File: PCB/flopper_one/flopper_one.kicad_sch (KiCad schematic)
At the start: 13 parts, among them J1 To PN532 ->, J2 <- ST7789, Q1 2N2219, SW1 SW_Omron_B3FS, SW2 SW_Omron_B3FS, SW3 SW_Omron_B3FS, SW4 SW_Omron_B3FS, SW5 SW_Omron_B3FS

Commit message: adfsdfd
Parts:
- U2: footprint ESP32_30pin -> wroom:MODULE_DEVKIT_V1_ESP32-WROOM-32
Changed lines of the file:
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@@
 			)
 		)
-		(property "Footprint" "ESP32_30pin"
+		(property "Footprint" "wroom:MODULE_DEVKIT_V1_ESP32-WROOM-32"
 			(at 156.21 89.5349 0)
 			(effects

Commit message: use labels
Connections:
- net VCC: no longer R1.2, U2.16 (3.3v)
- net P4: now reaches SW4.1, U2.4 (GPIO12)
- net P1: now reaches SW1.1, U2.5 (GPIO14)
- net P2: now reaches SW2.1, U2.6 (GPIO27)
- net P3: now reaches SW3.1, U2.7 (GPIO26)
- net P5: now reaches SW5.1, U2.8 (GPIO25)
- net SCL renamed SCL1
- net SCL1: no longer J2.3 (Pin_3), U2.24 (GPIO18)
- net SDA renamed SDA1
- net SDA1: no longer J2.4 (Pin_4), U2.25 (GPIO19)
- new net SCL2: J2.3 (Pin_3), U2.24 (GPIO18)
- new net SDA2: J2.4 (Pin_4), U2.25 (GPIO19)
- new net vcc: R1.2, U2.16 (3.3v)

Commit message: routed the pcb
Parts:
- J1: footprint Connector_PinHeader_1.00mm:PinHeader_1x04_P1.00mm_Vertical -> Connector_PinHeader_2.54mm:PinHeader_1x04_P2.54mm_Vertical
- J2: footprint Connector_PinHeader_1.00mm:PinHeader_1x07_P1.00mm_Vertical -> Connector_PinHeader_2.54mm:PinHeader_1x07_P2.54mm_Vertical
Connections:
- net vcc is gone; now on net VCC: R1.2, U2.16 (3.3v)
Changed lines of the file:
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@@
 		)
 	)
-	(label "vcc"
+	(label "VCC"
 		(at 147.32 72.39 0)
 		(effects
@@
 			)
 		)
-		(property "Footprint" "Connector_PinHeader_1.00mm:PinHeader_1x07_P1.00mm_Vertical"
+		(property "Footprint" "Connector_PinHeader_2.54mm:PinHeader_1x07_P2.54mm_Vertical"
 			(at 63.5 102.87 0)
 			(effects
@@
 			)
 		)
-		(property "Footprint" "Connector_PinHeader_1.00mm:PinHeader_1x04_P1.00mm_Vertical"
+		(property "Footprint" "Connector_PinHeader_2.54mm:PinHeader_1x04_P2.54mm_Vertical"
 			(at 63.5 77.47 0)
 			(effects

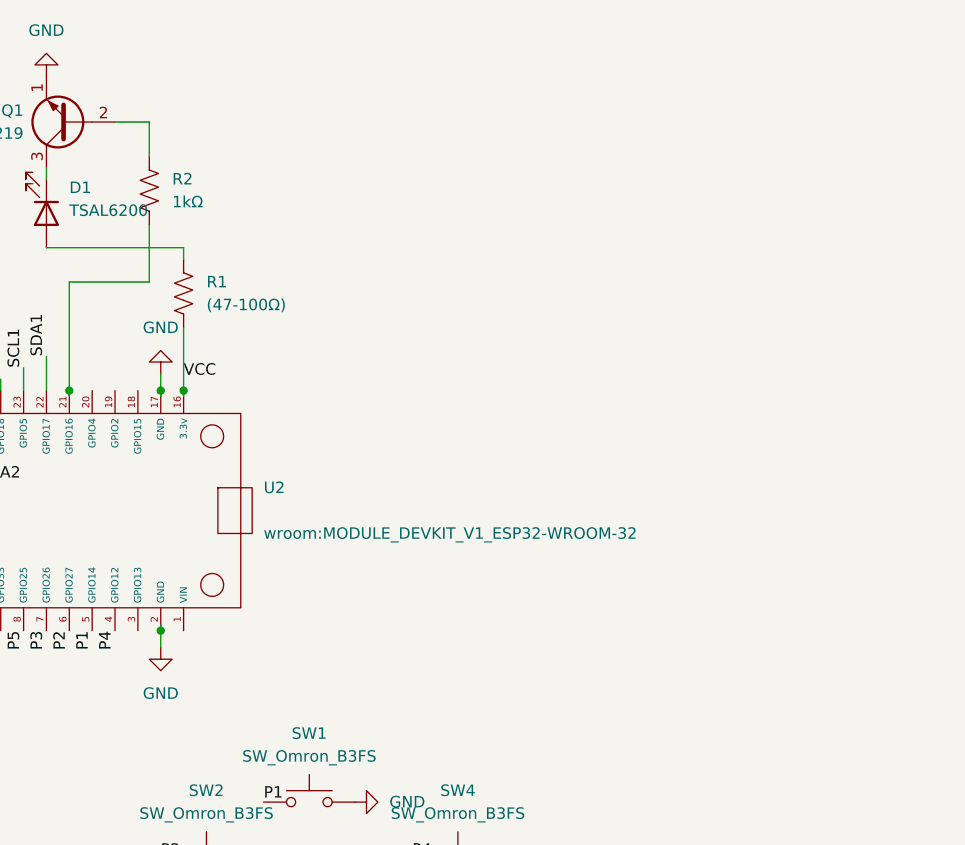
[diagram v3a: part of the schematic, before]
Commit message: add battery
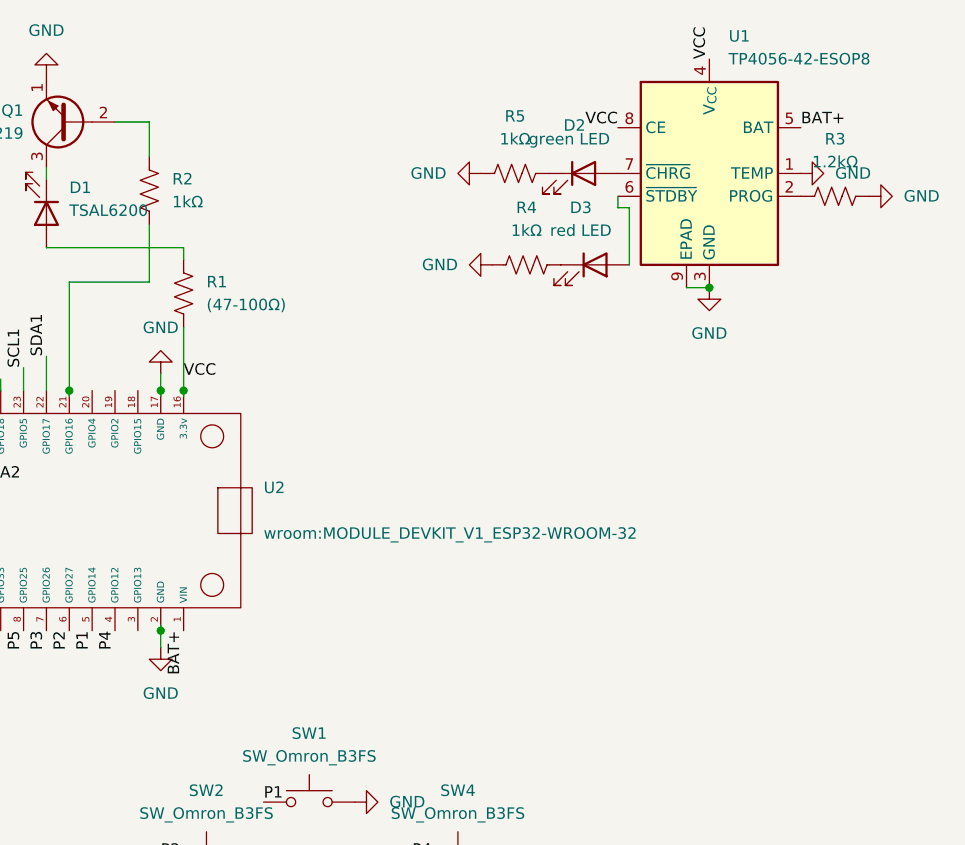
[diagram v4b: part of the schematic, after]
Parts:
- added D2: green LED, LED_THT:LED_D5.0mm, symbol Device:LED
- added D3: red LED, LED_THT:LED_D5.0mm, symbol Device:LED
- added R3: 1.2kΩ, Resistor_THT:R_Axial_DIN0207_L6.3mm_D2.5mm_P7.62mm_Horizontal, symbol Device:R_US
- added R4, R5: 1kΩ, Resistor_THT:R_Axial_DIN0207_L6.3mm_D2.5mm_P7.62mm_Horizontal, symbol Device:R_US
- added U1: TP4056-42-ESOP8, Package_SO:SOIC-8-1EP_3.9x4.9mm_P1.27mm_EP2.41x3.3mm_ThermalVias, symbol Battery_Management:TP4056-42-ESOP8
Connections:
- net GND: now also R3.2, R4.1, R5.1, U1.1 (TEMP), U1.3 (GND), U1.9 (EPAD)
- net VCC: now also U1.4 (V_{CC}), U1.8 (CE)
- net BAT+: now reaches U2.1 (VIN)
- net BAT+: now also U1.5 (BAT)
- new net: D3.1 (K), R4.2
- new net: D3.2 (A), U1.6 (~{STDBY})
- new net: R3.1, U1.2 (PROG)
- new net: D2.1 (K), R5.2
- new net: D2.2 (A), U1.7 (~{CHRG})

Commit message: added like power circuits fr
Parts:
- added C1: 10uf, Capacitor_THT:CP_Axial_L10.0mm_D4.5mm_P15.00mm_Horizontal, symbol Device:C_Small
- added U3: MT3608 module, MT3608:hw-045, symbol hw-045:hw-045
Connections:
- net BAT+: now also C1.1, U3.1 (VIN+); no longer U2.1 (VIN)
- net GND: now also D2.2 (A), D3.2 (A), C1.2, U3.2 (VIN-), U3.4 (VOUT-); no longer R4.1, R5.1
- net at U1.6 (~{STDBY}): now also R4.1; no longer D3.2 (A)
- net at U1.7 (~{CHRG}): now also R5.1; no longer D2.2 (A)
- new net VIN: U2.1 (VIN), U3.3 (VOUT+)
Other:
- moved on the sheet: D2, D3, R4, R5

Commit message: fix battery rq
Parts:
- removed U3: MT3608 module, MT3608:hw-045, symbol hw-045:hw-045
- added U4: hw-045, MT3608:hw-045, symbol hw-045:hw-045
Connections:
- net BAT+: now also U4.4 (VIN+)
- net GND: now also U4.2 (VOUT-), U4.3 (VIN-)
- net VIN: now also U4.1 (VOUT+)
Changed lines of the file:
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@@
+		)
+	)
+	(label "VIN"
+		(at 205.74 140.97 180)
+		(effects
+			(font
+				(size 1.27 1.27)
+			)
+			(justify right bottom)
 		)
 	)
@@
 		)
 	)
-	(label "BAT+"
-		(at 204.47 121.92 180)
-		(effects
-			(font
-				(size 1.27 1.27)
-			)
-			(justify right bottom)
-		)
-	)
 	(label "P1"
 		(at 156.21 119.38 0)
@@
 		)
 	)
-	(label "VIN"
-		(at 232.41 124.46 0)
-		(effects
-			(font
-				(size 1.27 1.27)
-			)
-			(justify left bottom)
-		)
-	)
 	(label "P5"
 		(at 106.68 125.73 0)
@@
 		)
 	)
+	(label "BAT+"
+		(at 233.68 140.97 0)
+		(effects
+			(font
+				(size 1.27 1.27)
+			)
+			(justify left bottom)
+		)
+	)
 	(label "SDA2"
 		(at 124.46 83.82 0)
@@
 	(symbol
 		(lib_id "power:GND")
-		(at 232.41 121.92 180)
-		(unit 1)
-		(exclude_from_sim no)
-		(in_bom yes)
-		(on_board yes)
-		(dnp no)
-		(fields_autoplaced yes)
-		(property "Reference" "#PWR019"
-			(at 232.41 115.57 0)
-			(effects
-				(font
-					(size 1.27 1.27)
-				)
-				(hide yes)
-			)
-		)
-		(property "Value" "GND"
-			(at 232.41 116.84 0)
-			(effects
-				(font
-					(size 1.27 1.27)
-				)
-			)
-		)
-		(property "Footprint" ""
-			(at 232.41 121.92 0)
-			(effects
-				(font
-					(size 1.27 1.27)
-				)
-				(hide yes)
-			)
-		)
-		(property "Datasheet" ""
-			(at 232.41 121.92 0)
-			(effects
-				(font
-					(size 1.27 1.27)
-				)
-				(hide yes)
-			)
-		)
-		(property "Description" "Power symbol creates a global label with name \"GND\" , ground"
-			(at 232.41 121.92 0)
-			(effects
-				(font
-					(size 1.27 1.27)
-				)
-				(hide yes)
-			)
-		)
-		(pin "1"
-		)
-		(instances
-			(project ""
-				(path "/8fc37294-f81b-4810-89c7-f789c9f89558"
-					(reference "#PWR019")
-					(unit 1)
-				)
-			)
-		)
-	)
-	(symbol
-		(lib_id "power:GND")
 		(at 166.37 119.38 90)
 		(unit 1)
@@
 	)
 	(symbol
+		(lib_id "hw-045:hw-045")
+		(at 218.44 143.51 0)
+		(unit 1)
+		(exclude_from_sim no)
+		(in_bom yes)
+		(on_board yes)
+		(dnp no)
+		(fields_autoplaced yes)
+		(property "Reference" "U4"
+			(at 219.71 133.35 0)
+			(effects
+				(font
+					(size 1.27 1.27)
+				)
+			)
+		)
+		(property "Value" "hw-045"
+			(at 219.71 135.89 0)
+			(effects
+				(font
+					(size 1.27 1.27)
+				)
+			)
+		)
+		(property "Footprint" "MT3608:hw-045"
+			(at 218.44 143.51 0)
+			(effects
+				(font
+					(size 1.27 1.27)
+				)
+				(hide yes)
+			)
+		)
+		(property "Datasheet" ""
+			(at 218.44 143.51 0)
+			(effects
+				(font
+					(size 1.27 1.27)
+				)
+				(hide yes)
+			)
+		)
+		(property "Description" ""
+			(at 218.44 143.51 0)
+			(effects
+				(font
+					(size 1.27 1.27)
+				)
+				(hide yes)
+			)
+		)
+		(pin "2"
+		)
+		(pin "1"
+		)
+		(pin "3"
+		)
+		(pin "4"
+		)
+		(instances
+			(project ""
+				(path "/8fc37294-f81b-4810-89c7-f789c9f89558"
+					(reference "U4")
+					(unit 1)
+				)
+			)
+		)
+	)
+	(symbol
 		(lib_id "power:GND")
 		(at 132.08 38.735 180)
@@
 	)
 	(symbol
-		(lib_id "hw-045:hw-045")
-		(at 217.17 124.46 0)
-		(unit 1)
-		(exclude_from_sim no)
-		(in_bom yes)
-		(on_board yes)
-		(dnp no)
-		(fields_autoplaced yes)
-		(property "Reference" "U3"
-			(at 218.44 114.3 0)
-			(effects
-				(font
-					(size 1.27 1.27)
-				)
-			)
-		)
-		(property "Value" "MT3608 module"
-			(at 218.44 116.84 0)
-			(effects
-				(font
-					(size 1.27 1.27)
-				)
-			)
-		)
-		(property "Footprint" "MT3608:hw-045"
-			(at 217.17 124.46 0)
-			(effects
-				(font
-					(size 1.27 1.27)
-				)
-				(hide yes)
-			)
-		)
-		(property "Datasheet" ""
-			(at 217.17 124.46 0)
-			(effects
-				(font
-					(size 1.27 1.27)
-				)
-				(hide yes)
-			)
-		)
-		(property "Description" ""
-			(at 217.17 124.46 0)
-			(effects
-				(font
-					(size 1.27 1.27)
-				)
-				(hide yes)
-			)
-		)
-		(pin "4"
-		)
-		(pin "3"
-		)
-		(pin "1"
-		)
-		(pin "2"
-		)
-		(instances
-			(project ""
-				(path "/8fc37294-f81b-4810-89c7-f789c9f89558"
-					(reference "U3")
-					(unit 1)
-				)
-			)
-		)
-	)
-	(symbol
 		(lib_id "Interface_Optical:TSOP382xx")
 		(at 96.52 56.515 0)
@@
 	(symbol
 		(lib_id "power:GND")
+		(at 205.74 143.51 0)
+		(unit 1)
+		(exclude_from_sim no)
+		(in_bom yes)
+		(on_board yes)
+		(dnp no)
+		(fields_autoplaced yes)
+		(property "Reference" "#PWR020"
+			(at 205.74 149.86 0)
+			(effects
+				(font
+					(size 1.27 1.27)
+				)
+				(hide yes)
+			)
+		)
+		(property "Value" "GND"
+			(at 205.74 148.59 0)
+			(effects
+				(font
+					(size 1.27 1.27)
+				)
+			)
+		)
+		(property "Footprint" ""
+			(at 205.74 143.51 0)
+			(effects
+				(font
+					(size 1.27 1.27)
+				)
+				(hide yes)
+			)
+		)
+		(property "Datasheet" ""
+			(at 205.74 143.51 0)
+			(effects
+				(font
+					(size 1.27 1.27)
+				)
+				(hide yes)
+			)
+		)
+		(property "Description" "Power symbol creates a global label with name \"GND\" , ground"
+			(at 205.74 143.51 0)
+			(effects
+				(font
+					(size 1.27 1.27)
+				)
+				(hide yes)
+			)
+		)
+		(pin "1"
+		)
+		(instances
+			(project ""
+				(path "/8fc37294-f81b-4810-89c7-f789c9f89558"
+					(reference "#PWR020")
+					(unit 1)
+				)
+			)
+		)
+	)
+	(symbol
+		(lib_id "power:GND")
 		(at 73.66 74.93 90)
 		(unit 1)
@@
 	)
 	(symbol
-		(lib_id "power:GND")
-		(at 204.47 124.46 0)
-		(unit 1)
-		(exclude_from_sim no)
-		(in_bom yes)
-		(on_board yes)
-		(dnp no)
-		(fields_autoplaced yes)
-		(property "Reference" "#PWR018"
-			(at 204.47 130.81 0)
-			(effects
-				(font
-					(size 1.27 1.27)
-				)
-				(hide yes)
-			)
-		)
-		(property "Value" "GND"
-			(at 204.47 129.54 0)
-			(effects
-				(font
-					(size 1.27 1.27)
-				)
-			)
-		)
-		(property "Footprint" ""
-			(at 204.47 124.46 0)
-			(effects
-				(font
-					(size 1.27 1.27)
-				)
-				(hide yes)
-			)
-		)
-		(property "Datasheet" ""
-			(at 204.47 124.46 0)
-			(effects
-				(font
-					(size 1.27 1.27)
-				)
-				(hide yes)
-			)
-		)
-		(property "Description" "Power symbol creates a global label with name \"GND\" , ground"
-			(at 204.47 124.46 0)
-			(effects
-				(font
-					(size 1.27 1.27)
-				)
-				(hide yes)
-			)
-		)
-		(pin "1"
-		)
-		(instances
-			(project ""
-				(path "/8fc37294-f81b-4810-89c7-f789c9f89558"
-					(reference "#PWR018")
-					(unit 1)
-				)
-			)
-		)
-	)
-	(symbol
 		(lib_id "Device:C_Small")
 		(at 231.14 44.45 0)
@@
 					(unit 1)
 				)
+			)
+		)
+	)
+	(symbol
+		(lib_id "power:GND")
+		(at 233.68 143.51 0)
+		(unit 1)
+		(exclude_from_sim no)
+		(in_bom yes)
+		(on_board yes)
+		(dnp no)
+		(fields_autoplaced yes)
+		(property "Reference" "#PWR021"
+			(at 233.68 149.86 0)
+			(effects
+				(font
+					(size 1.27 1.27)
+				)
+				(hide yes)
+			)
+		)
+		(property "Value" "GND"
+			(at 233.68 148.59 0)
+			(effects
+				(font
+					(size 1.27 1.27)
+				)
+			)
+		)
+		(property "Footprint" ""
+			(at 233.68 143.51 0)
+			(effects
+				(font
+					(size 1.27 1.27)
+				)
+				(hide yes)
+			)
+		)
+		(property "Datasheet" ""
+			(at 233.68 143.51 0)
+			(effects
+				(font
+					(size 1.27 1.27)
+				)
+				(hide yes)
+			)
+		)
+		(property "Description" "Power symbol creates a global label with name \"GND\" , ground"
+			(at 233.68 143.51 0)
+			(effects
+				(font
+					(size 1.27 1.27)
+				)
+				(hide yes)
+			)
+		)
+		(pin "1"
+		)
+		(instances
+			(project ""
+				(path "/8fc37294-f81b-4810-89c7-f789c9f89558"
+					(reference "#PWR021")
+					(unit 1)
+				)

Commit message: gerbers, bom
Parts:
- added SW6: SW_SPST, wroom:my_switch, symbol Switch:SW_SPST
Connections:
- net VCC: no longer U1.4 (V_{CC})
- net VIN: now also U1.4 (V_{CC}), SW6.1 (A); no longer U4.1 (VOUT+)
- new net: SW6.2 (B), U4.1 (VOUT+)
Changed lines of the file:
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@@
+	(wire
+		(pts
+			(xy 196.85 140.97) (xy 205.74 140.97)
+		)
+		(stroke
+			(width 0)
+			(type default)
+		)
+	)
 	(wire
 		(pts
@@
 		)
 	)
-	(label "VCC"
+	(label "VIN"
 		(at 205.74 36.83 90)
 		(effects
@@
 	)
 	(label "VIN"
-		(at 205.74 140.97 180)
+		(at 186.69 140.97 180)
 		(effects
 			(font
@@
 					(unit 1)
 				)
+			)
+		)
+	)
+	(symbol
+		(lib_id "Switch:SW_SPST")
+		(at 191.77 140.97 0)
+		(unit 1)
+		(exclude_from_sim no)
+		(in_bom yes)
+		(on_board yes)
+		(dnp no)
+		(fields_autoplaced yes)
+		(property "Reference" "SW6"
+			(at 191.77 134.62 0)
+			(effects
+				(font
+					(size 1.27 1.27)
+				)
+			)
+		)
+		(property "Value" "SW_SPST"
+			(at 191.77 137.16 0)
+			(effects
+				(font
+					(size 1.27 1.27)
+				)
+			)
+		)
+		(property "Footprint" "wroom:my_switch"
+			(at 191.77 140.97 0)
+			(effects
+				(font
+					(size 1.27 1.27)
+				)
+				(hide yes)
+			)
+		)
+		(property "Datasheet" "~"
+			(at 191.77 140.97 0)
+			(effects
+				(font
+					(size 1.27 1.27)
+				)
+				(hide yes)
+			)
+		)
+		(property "Description" "Single Pole Single Throw (SPST) switch"
+			(at 191.77 140.97 0)
+			(effects
+				(font
+					(size 1.27 1.27)
+				)
+				(hide yes)
+			)
+		)
+		(pin "2"
+		)
+		(pin "1"
+		)
+		(instances
+			(project ""
+				(path "/8fc37294-f81b-4810-89c7-f789c9f89558"
+					(reference "SW6")
+					(unit 1)
+				)

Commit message: fix minor error
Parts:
- added C2: 10uf, Capacitor_THT:CP_Axial_L10.0mm_D4.5mm_P15.00mm_Horizontal, symbol Device:C_Small
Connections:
- net BAT+: now also SW6.2 (B); no longer U4.4 (VIN+)
- net GND: now also C2.2
- net VCC: no longer U1.8 (CE)
- net VIN: now also U1.8 (CE), U4.1 (VOUT+), C2.1; no longer SW6.1 (A)
- new net: SW6.1 (A), U4.4 (VIN+)
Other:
- moved on the sheet: SW6
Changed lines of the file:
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@@
+	)
+	(junction
+		(at 196.85 140.97)
+		(diameter 0)
+		(color 0 0 0 0)
 	)
 	(junction
@@
 	(wire
 		(pts
+			(xy 186.69 140.97) (xy 196.85 140.97)
+		)
+		(stroke
+			(width 0)
+			(type default)
+		)
+	)
+	(wire
+		(pts
 			(xy 134.62 61.595) (xy 134.62 73.66)
 		)
@@
 	(wire
 		(pts
+			(xy 236.22 140.97) (xy 233.68 140.97)
+		)
+		(stroke
+			(width 0)
+			(type default)
+		)
+	)
+	(wire
+		(pts
 			(xy 143.51 43.815) (xy 139.7 43.815)
 		)
@@
 	(wire
 		(pts
+			(xy 247.65 140.97) (xy 246.38 140.97)
+		)
+		(stroke
+			(width 0)
+			(type default)
+		)
+	)
+	(wire
+		(pts
 			(xy 68.58 74.93) (xy 73.66 74.93)
 		)
@@
 		)
 	)
-	(label "VCC"
+	(label "VIN"
 		(at 195.58 44.45 180)
 		(effects
@@
 		)
 	)
+	(label "BAT+"
+		(at 247.65 140.97 0)
+		(effects
+			(font
+				(size 1.27 1.27)
+			)
+			(justify left bottom)
+		)
+	)
 	(label "SCL2"
 		(at 127 72.39 90)
@@
 	(label "VCC"
 		(at 80.01 77.47 0)
-		(effects
-			(font
-				(size 1.27 1.27)
-			)
-			(justify left bottom)
-		)
-	)
-	(label "BAT+"
-		(at 233.68 140.97 0)
 		(effects
 			(font
@@
 	(symbol
 		(lib_id "Switch:SW_SPST")
-		(at 191.77 140.97 0)
+		(at 241.3 140.97 0)
 		(unit 1)
 		(exclude_from_sim no)
@@
 		(fields_autoplaced yes)
 		(property "Reference" "SW6"
-			(at 191.77 134.62 0)
+			(at 241.3 134.62 0)
 			(effects
 				(font
@@
 		)
 		(property "Value" "SW_SPST"
-			(at 191.77 137.16 0)
+			(at 241.3 137.16 0)
 			(effects
 				(font
@@
 		)
 		(property "Footprint" "wroom:my_switch"
-			(at 191.77 140.97 0)
+			(at 241.3 140.97 0)
 			(effects
 				(font
@@
 		)
 		(property "Datasheet" "~"
-			(at 191.77 140.97 0)
+			(at 241.3 140.97 0)
 			(effects
 				(font
@@
 		)
 		(property "Description" "Single Pole Single Throw (SPST) switch"
-			(at 191.77 140.97 0)
+			(at 241.3 140.97 0)
 			(effects
 				(font
@@
 		)
 		(instances
-			(project ""
+			(project "flopper_one"
 				(path "/8fc37294-f81b-4810-89c7-f789c9f89558"
 					(reference "SW6")
@@
 	(symbol
 		(lib_id "power:GND")
+		(at 196.85 146.05 0)
+		(unit 1)
+		(exclude_from_sim no)
+		(in_bom yes)
+		(on_board yes)
+		(dnp no)
+		(fields_autoplaced yes)
+		(property "Reference" "#PWR018"
+			(at 196.85 152.4 0)
+			(effects
+				(font
+					(size 1.27 1.27)
+				)
+				(hide yes)
+			)
+		)
+		(property "Value" "GND"
+			(at 196.85 151.13 0)
+			(effects
+				(font
+					(size 1.27 1.27)
+				)
+			)
+		)
+		(property "Footprint" ""
+			(at 196.85 146.05 0)
+			(effects
+				(font
+					(size 1.27 1.27)
+				)
+				(hide yes)
+			)
+		)
+		(property "Datasheet" ""
+			(at 196.85 146.05 0)
+			(effects
+				(font
+					(size 1.27 1.27)
+				)
+				(hide yes)
+			)
+		)
+		(property "Description" "Power symbol creates a global label with name \"GND\" , ground"
+			(at 196.85 146.05 0)
+			(effects
+				(font
+					(size 1.27 1.27)
+				)
+				(hide yes)
+			)
+		)
+		(pin "1"
+		)
+		(instances
+			(project "flopper_one"
+				(path "/8fc37294-f81b-4810-89c7-f789c9f89558"
+					(reference "#PWR018")
+					(unit 1)
+				)
+			)
+		)
+	)
+	(symbol
+		(lib_id "power:GND")
 		(at 132.08 38.735 180)
 		(unit 1)
@@
 					(unit 1)
 				)
+			)
+		)
+	)
+	(symbol
+		(lib_id "Device:C_Small")
+		(at 196.85 143.51 0)
+		(unit 1)
+		(exclude_from_sim no)
+		(in_bom yes)
+		(on_board yes)
+		(dnp no)
+		(fields_autoplaced yes)
+		(property "Reference" "C2"
+			(at 199.39 142.2462 0)
+			(effects
+				(font
+					(size 1.27 1.27)
+				)
+				(justify left)
+			)
+		)
+		(property "Value" "10uf"
+			(at 199.39 144.7862 0)
+			(effects
+				(font
+					(size 1.27 1.27)
+				)
+				(justify left)
+			)
+		)
+		(property "Footprint" "Capacitor_THT:CP_Axial_L10.0mm_D4.5mm_P15.00mm_Horizontal"
+			(at 196.85 143.51 0)
+			(effects
+				(font
+					(size 1.27 1.27)
+				)
+				(hide yes)
+			)
+		)
+		(property "Datasheet" "~"
+			(at 196.85 143.51 0)
+			(effects
+				(font
+					(size 1.27 1.27)
+				)
+				(hide yes)
+			)
+		)
+		(property "Description" "Unpolarized capacitor, small symbol"
+			(at 196.85 143.51 0)
+			(effects
+				(font
+					(size 1.27 1.27)
+				)
+				(hide yes)
+			)
+		)
+		(pin "1"
+		)
+		(pin "2"
+		)
+		(instances
+			(project "flopper_one"
+				(path "/8fc37294-f81b-4810-89c7-f789c9f89558"
+					(reference "C2")
+					(unit 1)
+				)
